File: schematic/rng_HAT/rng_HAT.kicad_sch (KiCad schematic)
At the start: 32 parts, among them J1 RPi_GPIO, Q1 2N3904, Q2 2N3904, Q3 2N3904, Q4 BC107, Q5 2N3904, U3 STM32F103C8Tx

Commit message: some more PCB updates
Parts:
- removed C1: 10uF, Capacitor_SMD:CP_Elec_3x5.3, symbol Device:C_Polarized_Small_US
- removed C2: 0.1uF, Capacitor_SMD:CP_Elec_3x5.3, symbol Device:C_Polarized_Small_US
- removed C3: 100nF, Capacitor_SMD:CP_Elec_3x5.3, symbol Device:C_Polarized_Small_US
- removed C4: 2.2uF, Capacitor_SMD:CP_Elec_3x5.3, symbol Device:C_Polarized_Small_US
- added C1: 0.1uF, Capacitor_SMD:C_0603_1608Metric_Pad1.08x0.95mm_HandSolder, symbol Device:C_Small
- added C2: 2.2uF, Capacitor_SMD:C_0603_1608Metric_Pad1.08x0.95mm_HandSolder, symbol Device:C_Polarized_Small
- added C3, C8: 20pF, Capacitor_SMD:C_0603_1608Metric_Pad1.08x0.95mm_HandSolder, symbol Device:C_Small
- added C4: 100nF, Capacitor_SMD:C_0603_1608Metric_Pad1.08x0.95mm_HandSolder, symbol Device:C_Small
- added C6: 10uF, Capacitor_SMD:C_0603_1608Metric_Pad1.08x0.95mm_HandSolder, symbol Device:C_Small
- added C7: 104nF, Capacitor_SMD:C_0603_1608Metric_Pad1.08x0.95mm_HandSolder, symbol Device:C_Small
- added J2: Conn_01x04_Pin, Connector_PinHeader_1.00mm:PinHeader_1x04_P1.00mm_Horizontal, symbol Connector:Conn_01x04_Pin
- added R12: 1M, Resistor_SMD:R_0201_0603Metric, symbol Device:R
- added Y2: 8MHz, Crystal:Crystal_SMD_3215-2Pin_3.2x1.5mm, symbol ECS-80-S-4X:ECS-80-S-4X
- D4: value GRN (FW ON) -> GRN (PWR ON)
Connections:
- net 3V: now also C7.1, J2.1 (Pin_1)
- net 5V: now also C6.2
- net GND: now also C3.1, C6.1, C7.2, C8.1, J2.4 (Pin_4)
- net WN OUT: now also C2.2
- net at Q5.2 (B), R8.1: now also C4.2
- net at Q5.3 (C), R8.2, R9.1: now also C2.1
- net at Q3.2 (B), R2.2: now also C1.2
- net at Q1.1 (E), Q2.3 (C), R1.2: now also C1.1
- net at Q4.3 (C), R6.1: now also C4.1
- net at U3.34 (PA13): now also J2.2 (Pin_2)
- net at U3.37 (PA14): now also J2.3 (Pin_3)
- net at U3.5 (PD0): now also C8.2, R12.2, Y2.1
- net at U3.6 (PD1): now also C3.2, R12.1, Y2.2
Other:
- note added: "8Mhz Clock"
- note added: "JTAG/SWIO"

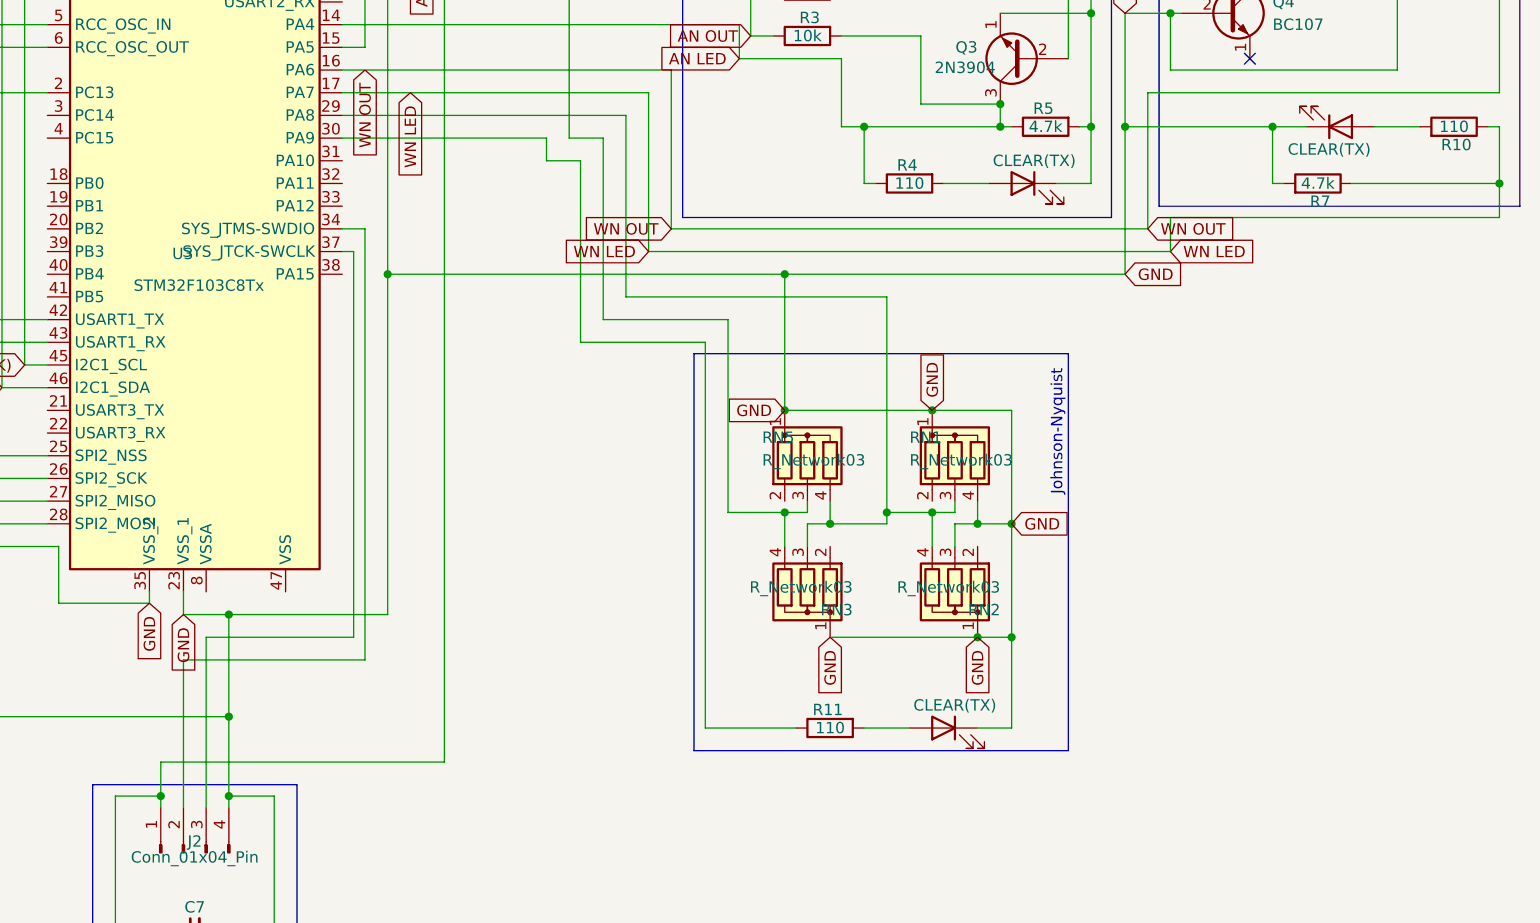
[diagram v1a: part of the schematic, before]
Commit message: updating schematic with white noise filter. no output stage? useful? need to test some of these components....
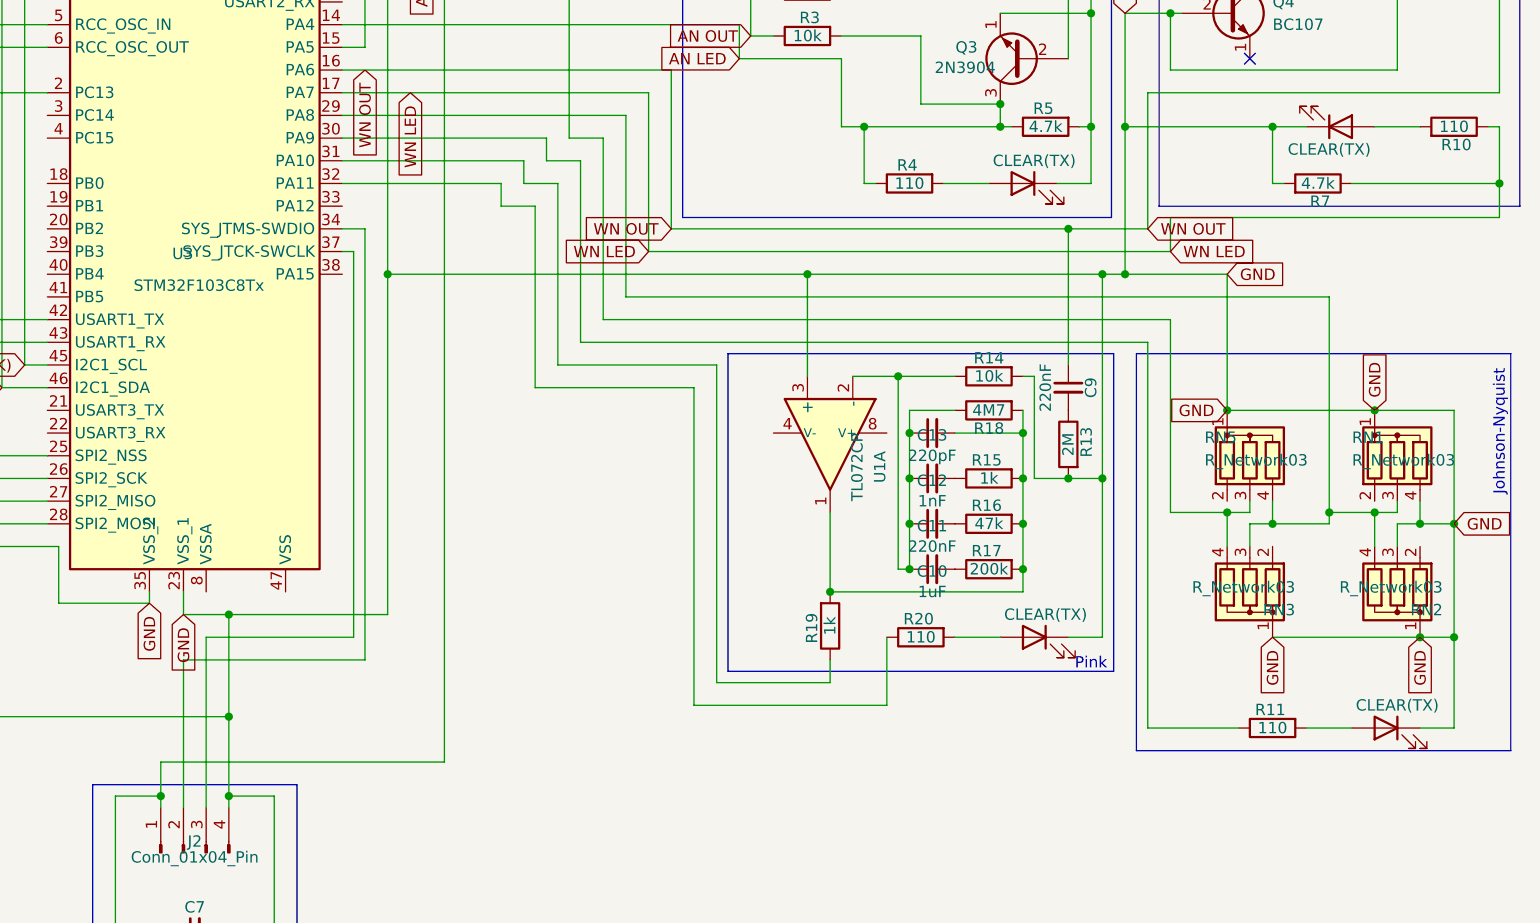
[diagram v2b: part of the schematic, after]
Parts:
- added C10: 1uF, Capacitor_SMD:C_0603_1608Metric_Pad1.08x0.95mm_HandSolder, symbol Device:C_Small
- added C11, C9: 220nF, Capacitor_SMD:C_0603_1608Metric_Pad1.08x0.95mm_HandSolder, symbol Device:C_Small
- added C12: 1nF, Capacitor_SMD:C_0603_1608Metric_Pad1.08x0.95mm_HandSolder, symbol Device:C_Small
- added C13: 220pF, Capacitor_SMD:C_0603_1608Metric_Pad1.08x0.95mm_HandSolder, symbol Device:C_Small
- added D6: CLEAR(TX), LED_SMD:LED_0201_0603Metric, symbol Device:LED
- added R13: 2M, Resistor_SMD:R_0201_0603Metric, symbol Device:R
- added R14: 10k, Resistor_SMD:R_0201_0603Metric, symbol Device:R
- added R15, R19: 1k, Resistor_SMD:R_0201_0603Metric, symbol Device:R
- added R16: 47k, Resistor_SMD:R_0201_0603Metric, symbol Device:R
- added R17: 200k, Resistor_SMD:R_0201_0603Metric, symbol Device:R
- added R18: 4M7, Resistor_SMD:R_0201_0603Metric, symbol Device:R
- added R20: 110, Resistor_SMD:R_0201_0603Metric, symbol Device:R
- added U1: TL072CP, PCM_Package_DIP_AKL:DIP-8_W7.62mm_LongPads, symbol PCM_Amplifier_Operational_AKL:TL072CP
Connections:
- net GND: now also D6.1 (K), R13.2, R14.2, U1.3 (+)
- net WN OUT: now also C9.1
- net at U3.31 (PA10): now also R19.1
- net at U3.32 (PA11): now also R20.1
- new net: C10.1, C11.1, C12.1, C13.1, R14.1, R18.1, U1.2 (-)
- new net: C13.2, R15.2, R16.2, R17.2, R18.2, R19.2, U1.1
- new net: D6.2 (A), R20.2
- new net: C10.2, R17.1
- new net: C9.2, R13.1
- new net: C12.2, R15.1
- new net: C11.2, R16.1
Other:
- note added: "Pink"
- moved on the sheet: R11, RN1, RN2, RN3, RN5

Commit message: PCB updates. holding  off on routes for now
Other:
- moved on the sheet: R20
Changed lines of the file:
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@@
 	(wire
 		(pts
-			(xy 236.22 114.3) (xy 232.41 114.3)
+			(xy 236.22 114.3) (xy 226.06 114.3)
 		)
 		(stroke
@@
 	(wire
 		(pts
-			(xy 219.71 114.3) (xy 224.79 114.3)
+			(xy 215.9 114.3) (xy 218.44 114.3)
 		)
 		(stroke
@@
 	(wire
 		(pts
-			(xy 190.5 121.92) (xy 212.09 121.92)
+			(xy 190.5 121.92) (xy 208.28 121.92)
 		)
 		(stroke
@@
 	(wire
 		(pts
-			(xy 212.09 121.92) (xy 212.09 114.3)
+			(xy 208.28 121.92) (xy 208.28 114.3)
 		)
 		(stroke
@@
 	)
 	(rectangle
-		(start 189.23 16.51)
+		(start 190.5 16.51)
 		(end 237.236 67.31)
 		(stroke
@@
 	(symbol
 		(lib_id "Device:R")
-		(at 215.9 114.3 90)
+		(at 212.09 114.3 90)
 		(mirror x)
 		(unit 1)
@@
 		(dnp no)
 		(property "Reference" "R20"
-			(at 215.646 112.268 90)
+			(at 211.836 112.268 90)
 			(effects
 				(font
@@
 		)
 		(property "Value" "110"
-			(at 215.9 114.3 90)
+			(at 212.09 114.3 90)
 			(effects
 				(font
@@
 		)
 		(property "Footprint" "Resistor_SMD:R_0201_0603Metric"
-			(at 215.9 112.522 90)
+			(at 212.09 112.522 90)
 			(effects
 				(font
@@
 		)
 		(property "Datasheet" "~"
-			(at 215.9 114.3 0)
+			(at 212.09 114.3 0)
 			(effects
 				(font
@@
 		)
 		(property "Description" "Resistor"
-			(at 215.9 114.3 0)
+			(at 212.09 114.3 0)
 			(effects
 				(font
@@
 	(symbol
 		(lib_id "Device:LED")
-		(at 228.6 114.3 0)
+		(at 222.25 114.3 0)
 		(mirror y)
 		(unit 1)
@@
 		(dnp no)
 		(property "Reference" "D6"
-			(at 230.1875 107.95 0)
+			(at 223.8375 107.95 0)
 			(effects
 				(font
@@
 		)
 		(property "Value" "CLEAR(TX)"
-			(at 229.87 111.76 0)
+			(at 223.52 111.76 0)
 			(effects
 				(font
@@
 		)
 		(property "Footprint" "LED_SMD:LED_0201_0603Metric"
-			(at 228.6 114.3 0)
+			(at 222.25 114.3 0)
 			(effects
 				(font
@@
 		)
 		(property "Datasheet" "~"
-			(at 228.6 114.3 0)
+			(at 222.25 114.3 0)
 			(effects
 				(font
@@
 		)
 		(property "Description" "Light emitting diode"
-			(at 228.6 114.3 0)
+			(at 222.25 114.3 0)
 			(effects
 				(font

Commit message: readme
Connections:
- net OSC_OUT: now reaches C3.2, R12.1, U3.6 (PD1), Y2.2
- net OSC_OUT: now also D1.2 (A), U3.2 (PC13)
- net OSC_IN: now reaches C8.2, R12.2, U3.5 (PD0), Y2.1
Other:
- title: (none) -> Random Number Generator Raspberry Pi HAT
- moved on the sheet: C1, C10, C11, C12, C13, C2, C3, C4, C5, C6, C7, C8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
